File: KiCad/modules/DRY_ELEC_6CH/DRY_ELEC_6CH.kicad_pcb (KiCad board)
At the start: 4 copper layers, 30 x 13 mm, 55 parts, among them J1 Conn_01x01_Pin, J10 Conn_01x01_Pin, J11 Conn_01x01_Pin, J12 Conn_01x01_Pin, J13 Conn_01x01_Pin, J14 Conn_01x01_Pin, J15 Conn_01x01_Pin, J16 Conn_01x01_Pin, J17 Conn_01x01_Pin, J18 Conn_01x01_Pin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

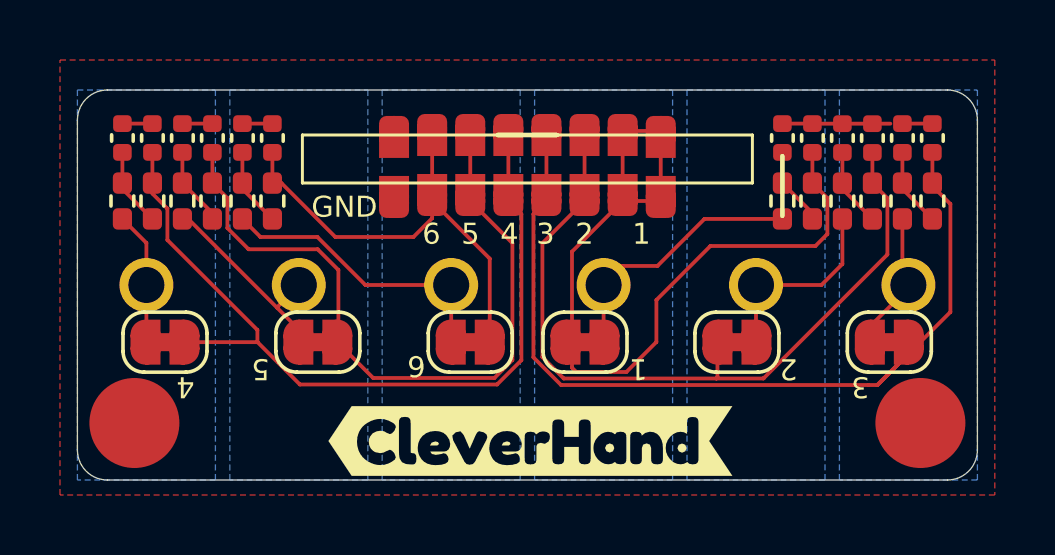
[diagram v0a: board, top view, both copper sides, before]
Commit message: added mid size to fit better with ads1293 module and standad xtal + some modificaion
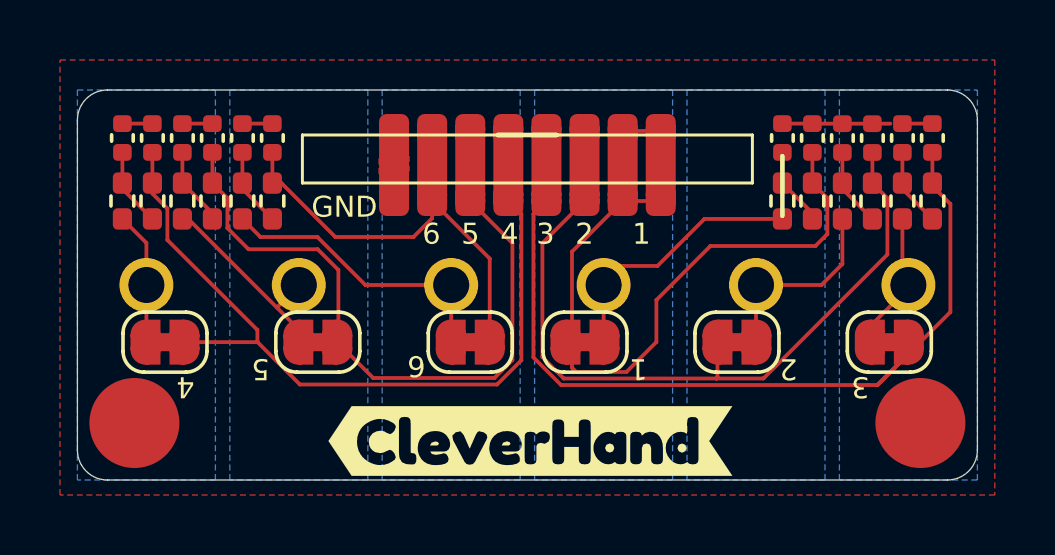
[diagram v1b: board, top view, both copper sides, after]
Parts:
- moved J16 0.07 mm to (34.4, 28.7)
- moved J9 0.07 mm to (25.6, 28.7)
- moved J1 0.06 mm to (25.6, 27.3)
- moved J8 0.06 mm to (34.4, 27.3)
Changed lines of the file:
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@@
 		(pad_to_mask_clearance 0)
 		(allow_soldermask_bridges_in_footprints no)
-		(grid_origin 29.999999 32)
+		(grid_origin 26.825 27.3)
 		(pcbplotparams
 			(layerselection 0x00010fc_ffffffff)
@@
 	(footprint "00_custom-footprints:SolderWirePad_1x01_SMD_1x2mm"
 		(layer "F.Cu")
-		(at 25.555 28.765 180)
+		(at 25.555 28.7 180)
 		(descr "Wire Pad, Square, SMD Pad,  1mm x 2mm,")
 		(tags "MesurementPoint Square SMDPad 1mmx2mm ")
@@
 	(footprint "00_custom-footprints:SolderWirePad_1x01_SMD_1x2mm"
 		(layer "F.Cu")
-		(at 34.445 28.765 180)
+		(at 34.445 28.7 180)
 		(descr "Wire Pad, Square, SMD Pad,  1mm x 2mm,")
 		(tags "MesurementPoint Square SMDPad 1mmx2mm ")
@@
 	(footprint "00_custom-footprints:SolderWirePad_1x01_SMD_1x2mm"
 		(layer "F.Cu")
-		(at 25.555 27.365)
+		(at 25.555 27.3)
 		(descr "Wire Pad, Square, SMD Pad,  1mm x 2mm,")
 		(tags "MesurementPoint Square SMDPad 1mmx2mm ")
@@
 	(footprint "00_custom-footprints:SolderWirePad_1x01_SMD_1x2mm"
 		(layer "F.Cu")
-		(at 34.445 27.365)
+		(at 34.445 27.3)
 		(descr "Wire Pad, Square, SMD Pad,  1mm x 2mm,")
 		(tags "MesurementPoint Square SMDPad 1mmx2mm ")
@@
 	)
 	(gr_rect
+		(start 31.405 27.7)
+		(end 32.405 28.3)
+		(stroke
+			(width 0)
+			(type solid)
+		)
+		(fill solid)
+		(layer "F.Cu")
+		(net 5)
+	)
+	(gr_rect
+		(start 33.945 27.7)
+		(end 34.945 28.3)
+		(stroke
+			(width 0)
+			(type solid)
+		)
+		(fill solid)
+		(layer "F.Cu")
+		(net 6)
+	)
+	(gr_rect
+		(start 27.595 27.7)
+		(end 28.595 28.3)
+		(stroke
+			(width 0)
+			(type solid)
+		)
+		(fill solid)
+		(layer "F.Cu")
+		(net 2)
+	)
+	(gr_rect
+		(start 32.675 27.7)
+		(end 33.675 28.3)
+		(stroke
+			(width 0)
+			(type solid)
+		)
+		(fill solid)
+		(layer "F.Cu")
+		(net 6)
+	)
+	(gr_rect
+		(start 28.865 27.7)
+		(end 29.865 28.3)
+		(stroke
+			(width 0)
+			(type solid)
+		)
+		(fill solid)
+		(layer "F.Cu")
+		(net 3)
+	)
+	(gr_rect
+		(start 25.055 27.7)
+		(end 26.055 28.3)
+		(stroke
+			(width 0)
+			(type solid)
+		)
+		(fill solid)
+		(layer "F.Cu")
+		(net 9)
+	)
+	(gr_rect
+		(start 26.325 27.7)
+		(end 27.325 28.3)
+		(stroke
+			(width 0)
+			(type solid)
+		)
+		(fill solid)
+		(layer "F.Cu")
+		(net 1)
+	)
+	(gr_rect
+		(start 30.135 27.7)
+		(end 31.135 28.3)
+		(stroke
+			(width 0)
+			(type solid)
+		)
+		(fill solid)
+		(layer "F.Cu")
+		(net 4)
+	)
+	(gr_rect
 		(start 22.5 27)
 		(end 37.5 28.6)
@@
 		(layer "B.Mask")
 	)
+	(gr_rect
+		(start 31.405 27.7)
+		(end 32.405 28.3)
+		(stroke
+			(width 0)
+			(type solid)
+		)
+		(fill solid)
+		(layer "F.Mask")
+	)
+	(gr_rect
+		(start 30.135 27.7)
+		(end 31.135 28.3)
+		(stroke
+			(width 0)
+			(type solid)
+		)
+		(fill solid)
+		(layer "F.Mask")
+	)
+	(gr_rect
+		(start 26.325 27.7)
+		(end 27.325 28.3)
+		(stroke
+			(width 0)
+			(type solid)
+		)
+		(fill solid)
+		(layer "F.Mask")
+	)
+	(gr_rect
+		(start 33.945 27.7)
+		(end 34.945 28.3)
+		(stroke
+			(width 0)
+			(type solid)
+		)
+		(fill solid)
+		(layer "F.Mask")
+	)
+	(gr_rect
+		(start 28.865 27.7)
+		(end 29.865 28.3)
+		(stroke
+			(width 0)
+			(type solid)
+		)
+		(fill solid)
+		(layer "F.Mask")
+	)
+	(gr_rect
+		(start 32.675 27.7)
+		(end 33.675 28.3)
+		(stroke
+			(width 0)
+			(type solid)
+		)
+		(fill solid)
+		(layer "F.Mask")
+	)
+	(gr_rect
+		(start 25.055 27.7)
+		(end 26.055 28.3)
+		(stroke
+			(width 0)
+			(type solid)
+		)
+		(fill solid)
+		(layer "F.Mask")
+	)
+	(gr_rect
+		(start 27.595 27.7)
+		(end 28.595 28.3)
+		(stroke
+			(width 0)
+			(type solid)
+		)
+		(fill solid)
+		(layer "F.Mask")
+	)
 	(gr_line
 		(start 14.999999 26.5)
@@
 	)
 	(gr_circle
+		(center 29.999999 28)
+		(end 30.199999 27.7)
+		(stroke
+			(width 0.1)
+			(type default)
+		)
+		(fill none)
+		(layer "F.Fab")
+	)
+	(gr_circle
 		(center 42.699999 32)
 		(end 43.969999 32)
@@
 	)
 	(zone
+		(net 9)
+		(net_name "GND")
+		(layer "F.Cu")
+		(hatch edge 0.5)
+		(priority 2)
+		(connect_pads
+			(clearance 0.127)
+		)
+		(min_thickness 0.25)
+		(filled_areas_thickness no)
+		(fill yes
+			(thermal_gap 0.5)
+			(thermal_bridge_width 0.5)
+		)
+		(polygon
+			(pts
+				(xy 25.055 27.7) (xy 26.055 27.7) (xy 26.055 28.3) (xy 25.055 28.3)
+			)
+		)
+	)
+	(zone
